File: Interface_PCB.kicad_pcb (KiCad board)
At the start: 2 copper layers, 53 parts, among them IC1 STM32L412RBT6P, J1 Conn_01x04, J2 Conn_01x04, J3 Conn_01x04, J4 Conn_01x04, J5 AVR-JTAG-10, J6 Micro_SD_Card, J7 USB_B, U1 AMS1117-3.3, Y1 Crystal, Y2 Crystal

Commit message: Layout Revision 1
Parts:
- removed C1, C2, C3: 22uF, Capacitor_SMD:C_0603_1608Metric
- removed C10, C11, C7, C8, C9: 100n, Capacitor_SMD:C_0603_1608Metric
- removed C13: 1u, Capacitor_SMD:C_0603_1608Metric
- removed C4, C5: 10n, Capacitor_SMD:C_0603_1608Metric
- removed C6: 4.7u, Capacitor_SMD:C_0805_2012Metric
- removed CSD1: 0.1uF, Capacitor_SMD:C_0402_1005Metric
- removed L2: 39nH, Capacitor_SMD:C_0603_1608Metric
- added G***: LOGO, motor-driver-test-board:parikshit_logo, F.Cu at (131.7, 97.3)
- added H1: MountingHole, MountingHole:MountingHole_2.1mm, F.Cu at (180.4, 148.0)
- added H2: MountingHole, MountingHole:MountingHole_2.1mm, F.Cu at (180.4, 142.2)
- added H3: MountingHole, MountingHole:MountingHole_2.1mm, F.Cu at (174.7, 142.2)
- added H4: MountingHole, MountingHole:MountingHole_2.1mm, F.Cu at (174.7, 148.0)
- CD1: footprint Capacitor_SMD:C_0805_2012Metric -> Capacitor_SMD:C_0402_1005Metric
- CD2, CD3, CD4, CD5, CD6: footprint Capacitor_SMD:C_0603_1608Metric -> Capacitor_SMD:C_0402_1005Metric
- CMS1, CMS2, CMS3: footprint Capacitor_SMD:C_0603_1608Metric -> Capacitor_SMD:C_0805_2012Metric
- D1, D2: footprint LED_SMD:LED_0603_1608Metric -> LED_SMD:LED_0805_2012Metric
- J1, J2, J3, J4: footprint Connector_Molex:Molex_CLIK-Mate_502382-0470_1x04-1MP_P1.25mm_Vertical -> SamacSys_Parts:502382-0470
- J7: footprint Connector_USB1:USB_Micro-B_Amphenol_10104110_Horizontal -> SamacSys_Parts:GMCB05B11124H1EU
- R1, R2: footprint Resistor_SMD:R_0603_1608Metric -> Resistor_SMD:R_0805_2012Metric
- moved LR1 130.7 mm to (178.7, 124.0), turned to -90 degrees
- moved CR2 128.6 mm to (175.7, 127.0), turned to -90 degrees
- moved CR1 125.5 mm to (175.7, 124.0), turned to -90 degrees
- moved NT1 124.0 mm to (178.7, 115.3), turned to -90 degrees
- moved CR3 121.5 mm to (177.2, 124.0), turned to -90 degrees
- moved U1 113.6 mm to (170.6, 126.0), turned to 180 degrees
- moved D1 97.5 mm to (168.6, 118.3), turned to 90 degrees
- moved J7 94.3 mm to (177.9, 103.5), turned to 90 degrees
- moved CB1 87.1 mm to (147.2, 96.0)
- moved CB3 86.6 mm to (160.4, 98.5)
- moved D2 86.1 mm to (164.5, 118.1), turned to 90 degrees
- moved R2 82.0 mm to (164.5, 114.6), turned to -90 degrees
- moved CB4 80.3 mm to (154.3, 116.3), turned to 180 degrees
- moved CB2 73.5 mm to (147.7, 115.3), turned to 180 degrees
- moved R1 66.2 mm to (168.6, 114.2), turned to -90 degrees
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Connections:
- CMS1 pad 2: Net-(CMS1-Pad2) -> GND
- CMS2 pad 2: Net-(CMS1-Pad2) -> GND
- CMS3 pad 2: Net-(CMS1-Pad2) -> GND
- CR1 pad 2: Net-(CR1-Pad2) -> GND
- CR2 pad 2: Net-(CR1-Pad2) -> GND
- CR3 pad 2: Net-(CR1-Pad2) -> GND
- J3 pad 2: I2C2_SCL -> I2C2_SDA
- J3 pad 3: I2C2_SDA -> I2C2_SCL
- U1 pad 1: Net-(CR1-Pad2) -> GND
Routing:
- net GND: track 0.00 -> 109.6 mm, vias 0 -> 22
- net SPI1_MOSI: track 0.00 -> 25.1 mm, vias 0 -> 2
- net +3V3: track 0.00 -> 24.0 mm
- net I2C1_SDA: track 0.00 -> 22.8 mm
- net I2C1_SCL: track 0.00 -> 22.8 mm
- net USART2_RX: track 0.00 -> 22.4 mm
- net USART2_TX: track 0.00 -> 22.2 mm
- net USB_D-: track 0.00 -> 20.8 mm
- net USB_D+: track 0.00 -> 20.7 mm
- net JTMS: track 0.00 -> 19.3 mm
- net SPI1_MISO: track 0.00 -> 18.7 mm, vias 0 -> 2
- net VBUS: track 0.00 -> 18.3 mm
- net JTCK: track 0.00 -> 17.8 mm, vias 0 -> 2
- net JTDO: track 0.00 -> 16.2 mm
- net I2C2_SCL: track 0.00 -> 14.9 mm
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- added copper zone on F.Cu, net +3V3
- added copper zone on B.Cu, net GND
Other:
- board outline added: 59.5 x 48.4 mm
- board text added: "47mm"
- board text added: "60mm"

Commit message: Layout rev2.0
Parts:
- removed G***: LOGO, motor-driver-test-board:parikshit_logo
- moved H1 146.1 mm to (77.4, 44.5)
- moved H2 145.1 mm to (66.3, 52.7)
- moved H3 138.7 mm to (96.1, 28.0)
- moved H4 137.6 mm to (86.2, 42.5)
- moved J6 29.3 mm to (154.8, 142.5)
- moved CMS2 24.9 mm to (144.1, 133.8), turned to -90 degrees
- moved CB1 23.1 mm to (143.2, 118.8), turned to -90 degrees
- moved CMS1 23.1 mm to (147.8, 133.1), turned to 0 degrees
- moved J1 21.7 mm to (168.2, 145.1)
- moved Y2 21.4 mm to (139.6, 125.2)
- moved CD1 21.0 mm to (146.8, 119.0), turned to -90 degrees
- moved Cl3 20.2 mm to (143.9, 126.8), turned to -90 degrees
- moved CMS3 19.5 mm to (145.6, 129.0)
- moved RExt1 19.2 mm to (145.5, 125.4), turned to -90 degrees
- moved Cl2 18.7 mm to (147.2, 114.5), turned to 180 degrees
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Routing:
- net GND: track 109.6 -> 0.00 mm, vias 22 -> 0
- net SPI1_MOSI: track 25.1 -> 0.00 mm, vias 2 -> 0
- net +3V3: track 24.0 -> 0.00 mm
- net I2C1_SDA: track 22.8 -> 0.00 mm
- net I2C1_SCL: track 22.8 -> 0.00 mm
- net USART2_RX: track 22.4 -> 0.00 mm
- net USART2_TX: track 22.2 -> 0.00 mm
- net USB_D-: track 20.8 -> 0.00 mm
- net USB_D+: track 20.7 -> 0.00 mm
- net JTMS: track 19.3 -> 0.00 mm
- net SPI1_MISO: track 18.7 -> 0.00 mm, vias 2 -> 0
- net VBUS: track 18.3 -> 0.00 mm
- net JTCK: track 17.8 -> 0.00 mm, vias 2 -> 0
- net JTDO: track 16.2 -> 0.00 mm
- net I2C2_SCL: track 14.9 -> 0.00 mm
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- removed copper zone on F.Cu, net +3V3
- removed copper zone on B.Cu, net GND
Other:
- board outline removed
- board text removed: "47mm"
- board text removed: "60mm"

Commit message: Layout rev3.0 - redesigned
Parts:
- added G***: LOGO, motor-driver-test-board:parikshit_logo, F.Cu at (121.0, 122.9)
- moved H4 111.7 mm to (158.0, 128.1)
- moved H2 90.6 mm to (116.7, 128.0)
- moved H1 87.7 mm to (157.4, 80.4)
- moved H3 56.0 mm to (116.6, 80.1)
- moved D1 29.4 mm to (151.5, 92.9), turned to 180 degrees
- moved R1 29.3 mm to (147.3, 92.8)
- moved R2 28.5 mm to (151.7, 84.5), turned to -90 degrees
- moved CMS1 27.0 mm to (129.1, 113.7)
- moved LR1 27.0 mm to (150.1, 111.0)
- moved Cl3 27.0 mm to (125.2, 107.3)
- moved LMS1 27.0 mm to (127.1, 111.5)
- moved CMS2 27.0 mm to (125.4, 114.4)
- moved CB1 27.0 mm to (124.6, 99.3)
- moved CB2 27.0 mm to (132.8, 112.8)
- moved CB3 27.0 mm to (132.3, 91.8)
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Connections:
- J6 pad 5: CLK -> SPI1_CLK
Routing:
- net GND: track 0.00 -> 107.3 mm, vias 0 -> 20
- net +3V3: track 0.00 -> 80.7 mm, vias 0 -> 4
- net I2C1_SDA: track 0.00 -> 35.4 mm
- net USART2_RX: track 0.00 -> 31.6 mm, vias 0 -> 2
- net USART2_TX: track 0.00 -> 29.2 mm, vias 0 -> 2
- net VBUS: track 0.00 -> 28.1 mm, vias 0 -> 2
- net I2C1_SCL: track 0.00 -> 27.0 mm
- net I2C2_SDA: track 0.00 -> 23.6 mm, vias 0 -> 2
- net I2C2_SCL: track 0.00 -> 21.7 mm, vias 0 -> 2
- net SPI1_CLK: track 0.00 -> 19.5 mm, vias 0 -> 2
- net JTDO: track 0.00 -> 17.2 mm
- net JTDI: track 0.00 -> 16.4 mm, vias 0 -> 2
- net USART1_RX: track 0.00 -> 16.4 mm
- net USART1_TX: track 0.00 -> 16.1 mm
- net JTMS: track 0.00 -> 16.0 mm
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- added copper zone on F.Cu, net +3V3
- added copper zone on B.Cu, net GND
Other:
- board outline added: 46.3 x 52.9 mm
- board text added: "P. ABHINAV M. CHINMAY"

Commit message: Design rev4.0
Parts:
- J5: footprint Connector_PinHeader_2.54mm:PinHeader_2x05_P2.54mm_Vertical_SMD -> SamacSys_Parts:FTSH10501LDVK
- moved J5 6.55 mm to (140.1, 89.7), turned to 0 degrees
- moved R2 6.42 mm to (147.3, 89.2), turned to 0 degrees
- moved J2 5.31 mm to (129.6, 88.3)
- moved H3 5.16 mm to (116.6, 85.3)
- moved H1 5.00 mm to (157.8, 85.4)
- moved D2 1.03 mm to (151.5, 89.2), turned to 180 degrees
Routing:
- net +3V3: track 80.7 -> 103.2 mm
- net GND: track 107.3 -> 88.0 mm, vias 20 -> 24
- net I2C1_SCL: track 27.0 -> 39.8 mm
- net JTDI: track 16.4 -> 11.7 mm, vias 2 -> 0
- net I2C1_SDA: track 35.4 -> 40.1 mm
- net JTDO: track 17.2 -> 12.9 mm
- net JTCK: track 11.8 -> 8.32 mm
- net USART1_RX: track 16.4 -> 12.9 mm
- net JTMS: track 16.0 -> 19.4 mm
- net Net-(CR1-Pad1): track 11.6 -> 14.1 mm
- net USART1_TX: track 16.1 -> 14.1 mm
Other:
- board size 46.3 x 52.9 mm -> 46.3 x 47.7 mm

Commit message: got rid of gnd parasitic vias around USB diff pair
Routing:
- net GND: vias 24 -> 20
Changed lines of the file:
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@@
   (via (at 143.764 86.0298) (size 0.8) (drill 0.4) (layers "F.Cu" "B.Cu") (net 2))
   (via (at 152.4254 122.0724) (size 0.8) (drill 0.4) (layers "F.Cu" "B.Cu") (net 2))
-  (via (at 147.574 100.2479) (size 0.5) (drill 0.3) (layers "F.Cu" "B.Cu") (free) (net 2))
   (via (at 127.635 86.0044) (size 0.8) (drill 0.4) (layers "F.Cu" "B.Cu") (net 2))
   (via (at 154.4066 92.5576) (size 0.8) (drill 0.4) (layers "F.Cu" "B.Cu") (net 2))
@@
   (via (at 133.4008 99.1616) (size 0.8) (drill 0.4) (layers "F.Cu" "B.Cu") (net 2))
   (via (at 138.4046 122.3518) (size 0.8) (drill 0.4) (layers "F.Cu" "B.Cu") (net 2))
-  (via (at 143.9164 100.2479) (size 0.5) (drill 0.3) (layers "F.Cu" "B.Cu") (free) (net 2))
-  (via (at 143.9926 101.7969) (size 0.5) (drill 0.3) (layers "F.Cu" "B.Cu") (free) (net 2))
   (via (at 127.254 94.3102) (size 0.8) (drill 0.4) (layers "F.Cu" "B.Cu") (net 2))
   (via (at 124.587 101.1936) (size 0.8) (drill 0.4) (layers "F.Cu" "B.Cu") (net 2))
@@
   (via (at 151.0792 114.2492) (size 0.8) (drill 0.4) (layers "F.Cu" "B.Cu") (net 2))
   (via (at 117.4242 117.3226) (size 0.8) (drill 0.4) (layers "F.Cu" "B.Cu") (net 2))
-  (via (at 147.701 101.8286) (size 0.5) (drill 0.3) (layers "F.Cu" "B.Cu") (free) (net 2))
   (via (at 131.6228 104.8004) (size 0.8) (drill 0.4) (layers "F.Cu" "B.Cu") (net 2))
   (via (at 152.8572 124.5362) (size 0.8) (drill 0.4) (layers "F.Cu" "B.Cu") (net 2))

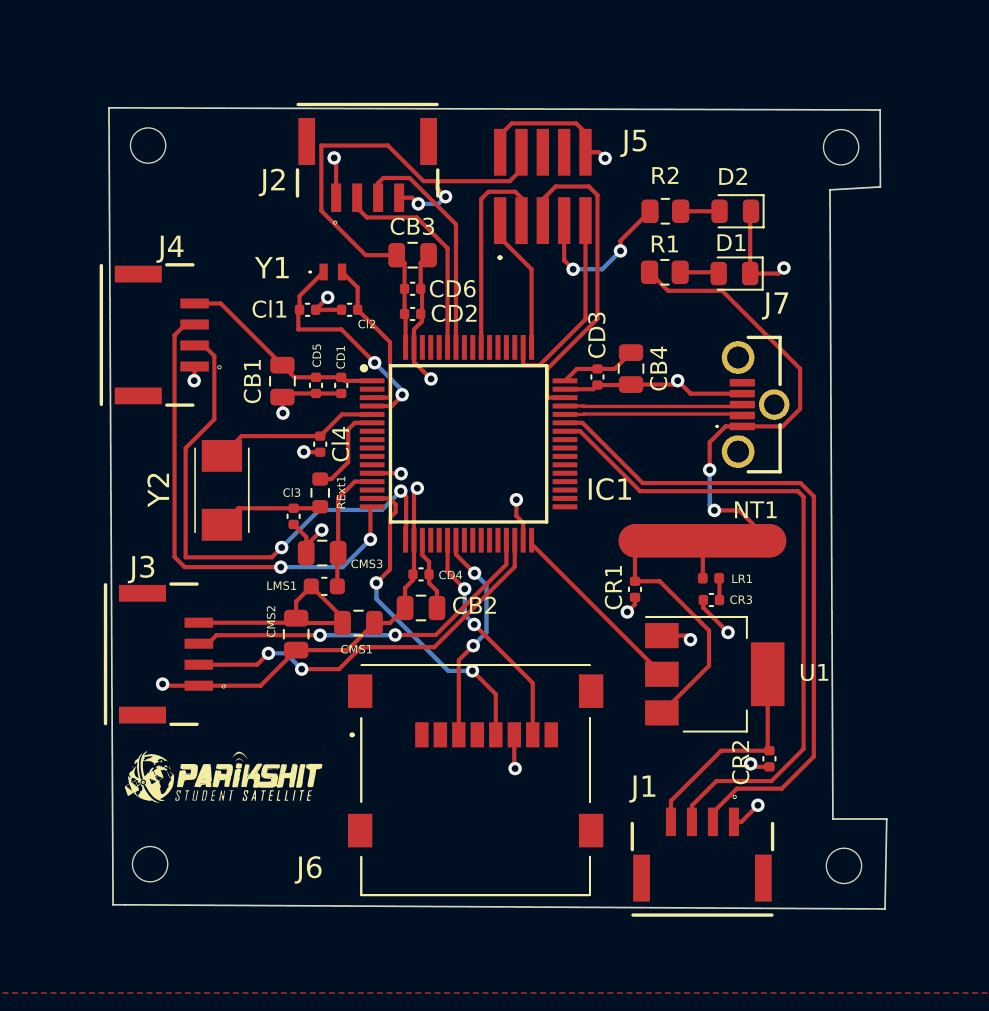
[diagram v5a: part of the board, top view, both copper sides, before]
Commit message: Edge cuts are improved
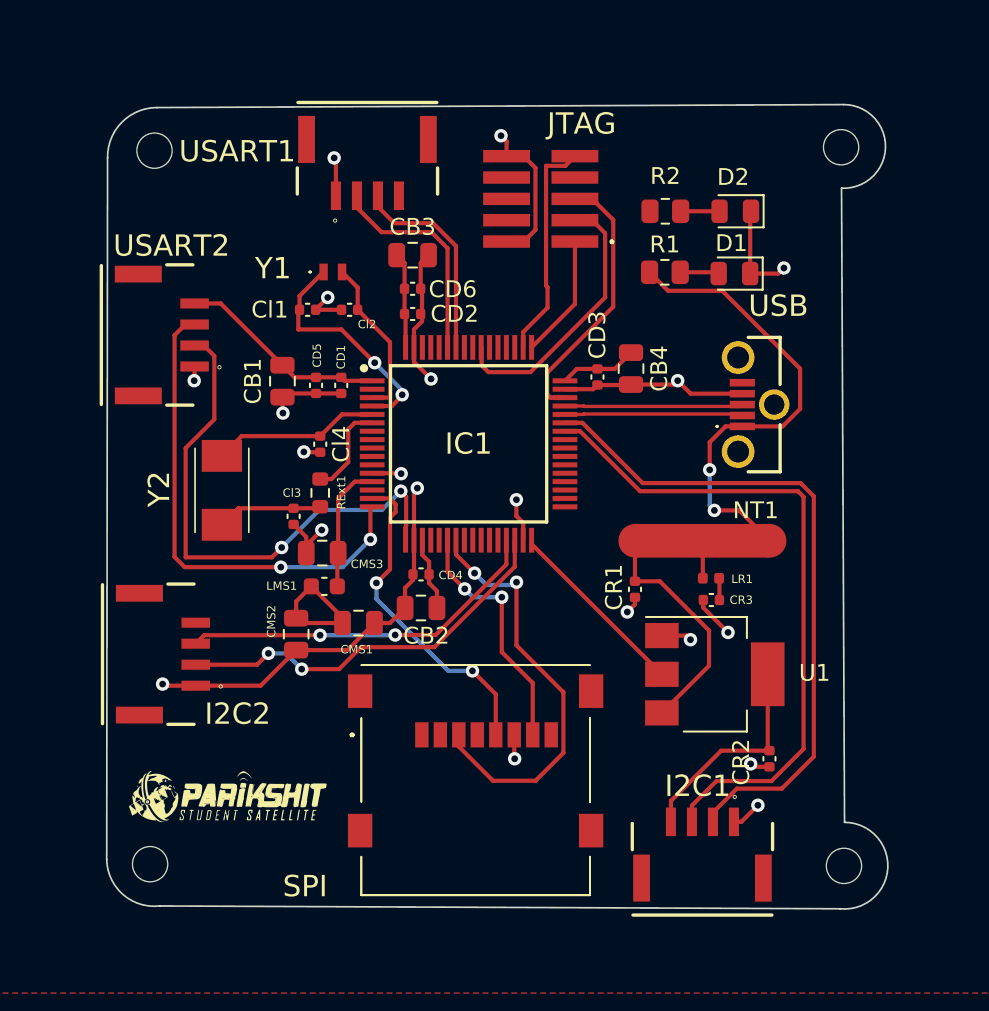
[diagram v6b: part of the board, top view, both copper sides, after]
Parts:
- moved JTAG 2.31 mm to (142.0, 88.4), turned to 90 degrees
- moved G*** 1.19 mm to (121.3, 124.0)
- moved H3 0.49 mm to (116.9, 85.6)
- moved I2C2 0.18 mm to (119.3, 115.5)
- moved USART1 0.12 mm to (129.6, 88.2)
- renumbered J1 to I2C1, J3 to I2C2, J5 to JTAG, J6 to SPI, J2 to USART1, J4 to USART2, J7 to USB
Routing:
- net +3V3: track 103.2 -> 60.0 mm, vias 4 -> 0
- net SPI1_MOSI: track 13.0 -> 25.0 mm
- net JTDO: track 12.9 -> 16.4 mm
- net JTMS: track 19.4 -> 15.9 mm
- net JTDI: track 11.7 -> 13.4 mm
- net USART1_TX: track 14.1 -> 12.9 mm
- net SPI1_MISO: track 13.7 -> 14.7 mm
- net JTCK: track 8.32 -> 7.37 mm
- net USART1_RX: track 12.9 -> 13.6 mm
- net GND: track 88.0 -> 87.4 mm
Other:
- board size 46.3 x 47.7 mm -> 46.5 x 47.9 mm

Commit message: Design rev 4.1
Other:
- board size 46.5 x 47.9 mm -> 47.1 x 48.4 mm
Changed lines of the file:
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@@
   )
   (gr_arc (start 114.1476 86.0044) (mid 114.992411 83.888061) (end 117.094 83.0072) (layer "Edge.Cuts") (width 0.1))
-  (gr_line (start 157.8356 87.8078) (end 158.0134 125.5522) (layer "Edge.Cuts") (width 0.1))
   (gr_line (start 117.2464 130.5306) (end 157.74826 130.69726) (layer "Edge.Cuts") (width 0.1))
-  (gr_arc (start 157.9626 82.8294) (mid 160.452609 85.38374) (end 157.8356 87.8078) (layer "Edge.Cuts") (width 0.1))
-  (gr_arc (start 158.0134 125.5522) (mid 160.589699 128.264326) (end 157.74826 130.69726) (layer "Edge.Cuts") (width 0.1))
+  (gr_arc (start 157.9626 82.8294) (mid 159.786145 83.611178) (end 160.4772 85.471) (layer "Edge.Cuts") (width 0.1))
+  (gr_arc (start 161.149494 128.919527) (mid 160.2486 130.7084) (end 158.318954 131.245187) (layer "Edge.Cuts") (width 0.1))
   (gr_line (start 114.0968 127.7366) (end 114.1476 86.0044) (layer "Edge.Cuts") (width 0.1))
   (gr_line (start 117.094 83.0072) (end 157.9626 82.8294) (layer "Edge.Cuts") (width 0.1))
+  (gr_line (start 160.4772 85.217) (end 160.5788 128.3716) (layer "Edge.Cuts") (width 0.1))
   (gr_arc (start 117.2464 130.5306) (mid 115.050113 129.834185) (end 114.0968 127.7366) (layer "Edge.Cuts") (width 0.1))
   (gr_text "P. ABHINAV\nM. CHINMAY" (at 123.698 127.889) (layer "B.SilkS")

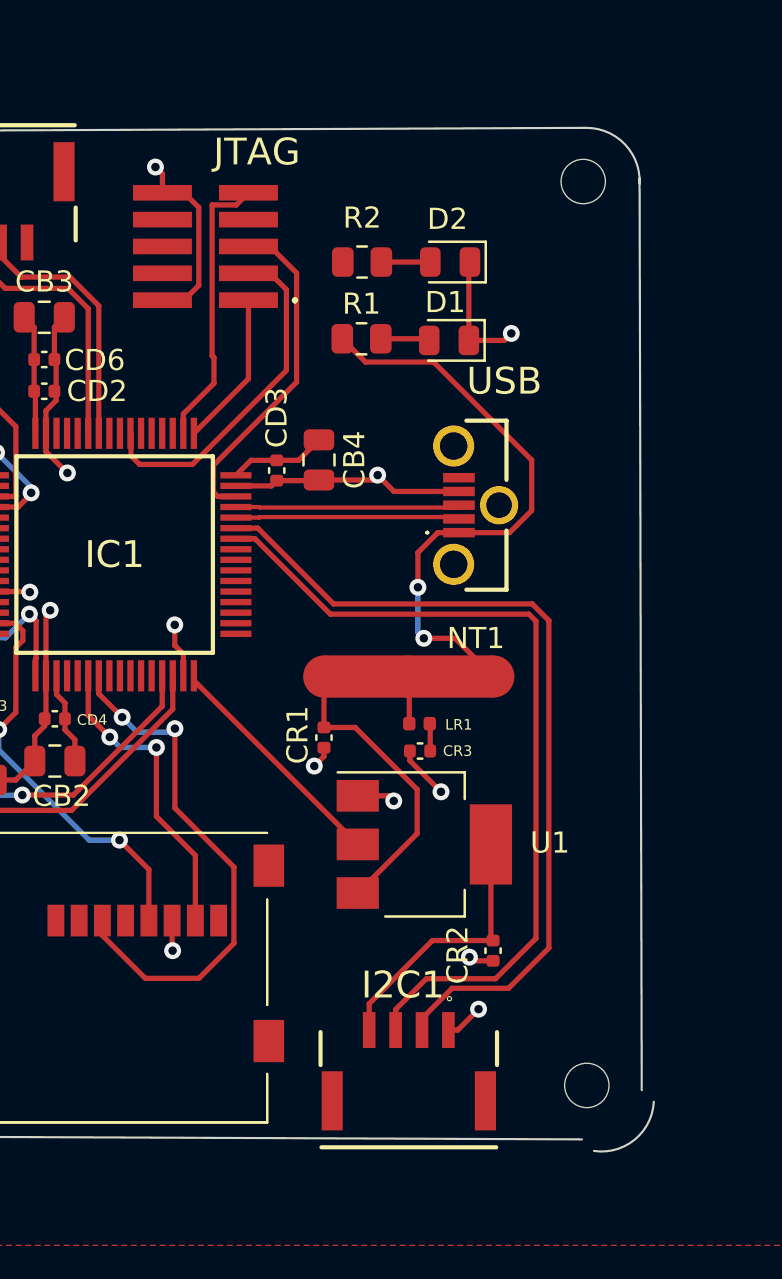
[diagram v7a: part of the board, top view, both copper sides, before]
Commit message: Resistor pads to SD card connector
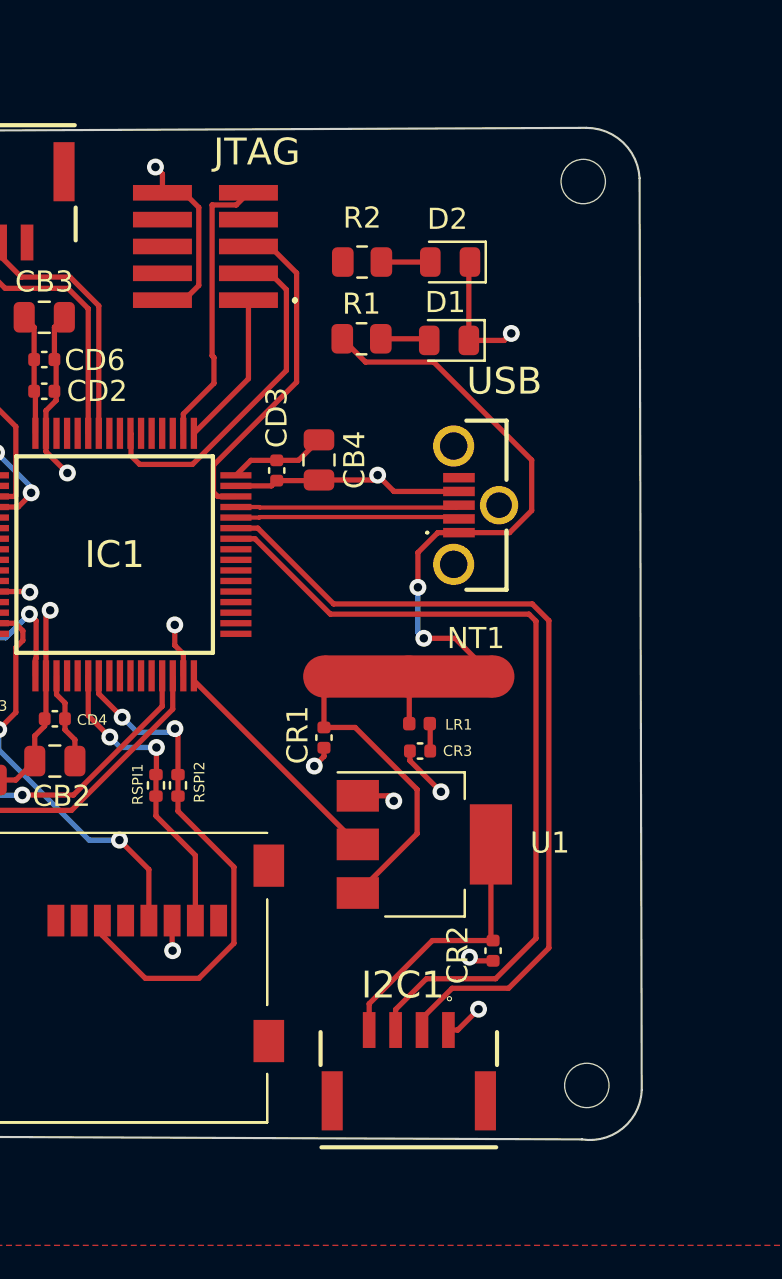
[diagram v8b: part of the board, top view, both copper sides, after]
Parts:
- added RSPI1: 1K, Resistor_SMD:R_0402_1005Metric, F.Cu at (137.6, 113.9)
- added RSPI2: 1K, Resistor_SMD:R_0402_1005Metric, F.Cu at (138.6, 113.9)
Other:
- board size 47.1 x 48.4 mm -> 46.5 x 47.9 mm
